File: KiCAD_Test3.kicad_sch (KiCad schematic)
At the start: 0 parts

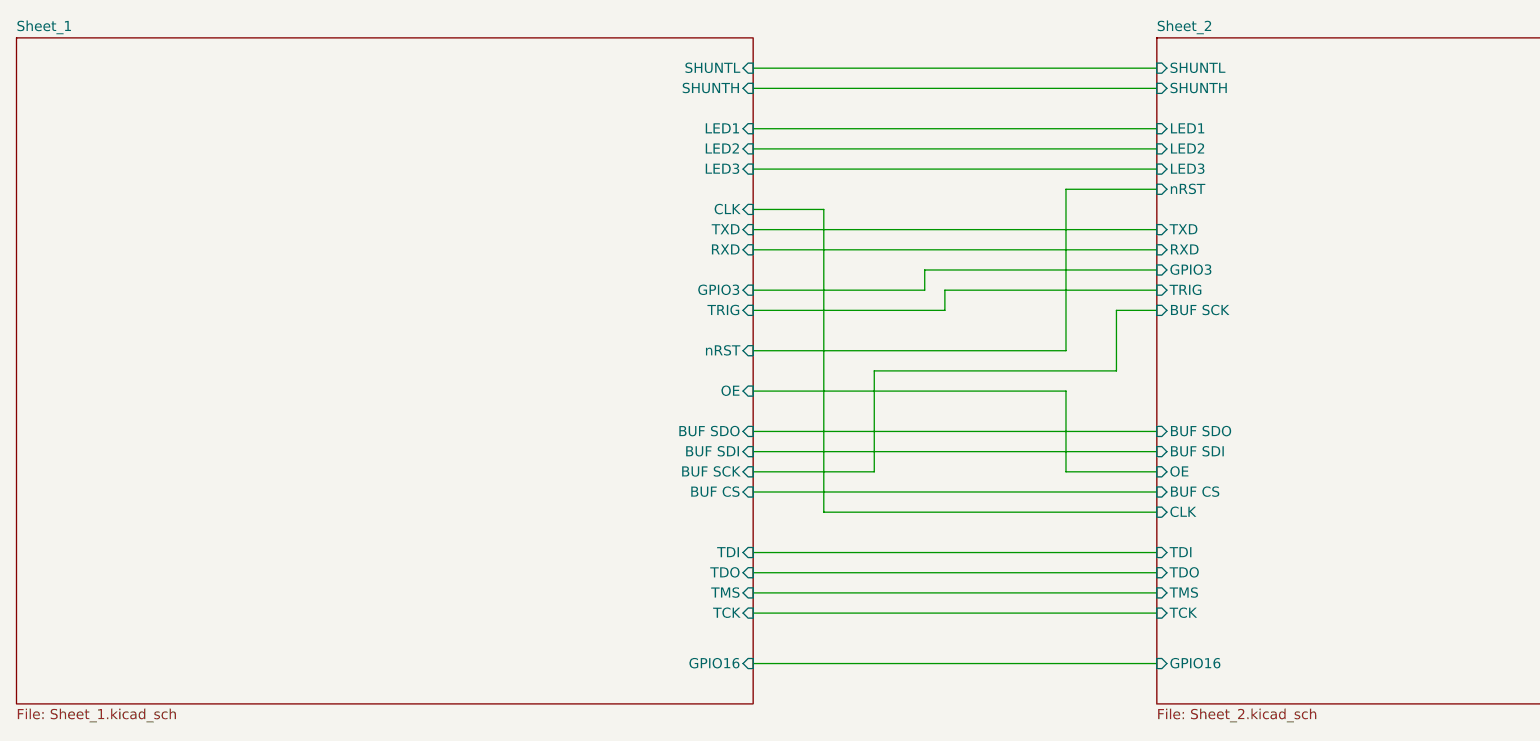
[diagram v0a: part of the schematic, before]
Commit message: updated ESP32 design - needs silkscreen added and shunt should be moved to be closer to U1
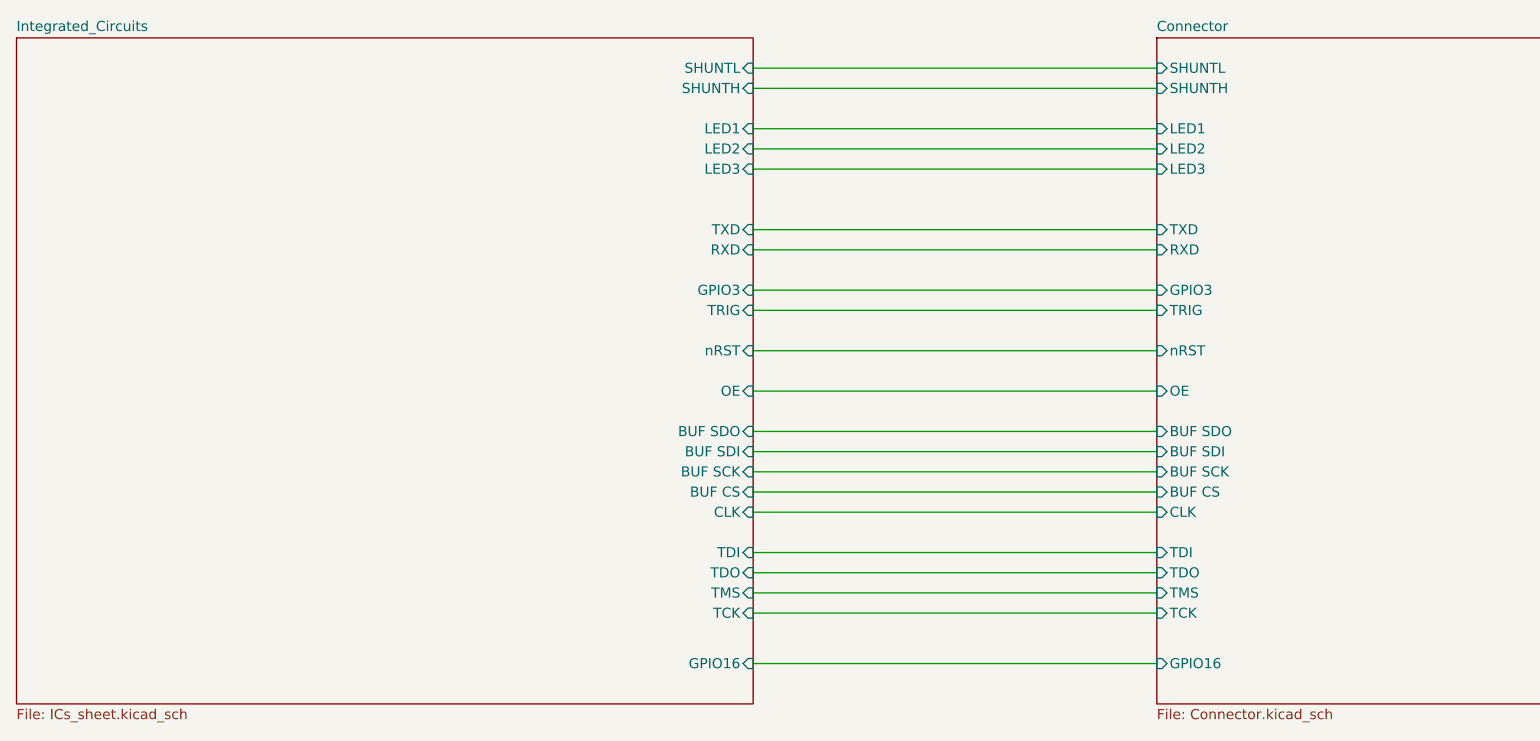
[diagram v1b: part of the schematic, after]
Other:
- sheet Sheet_1 renamed Integrated_Circuits
- sheet Sheet_2 renamed Connector
- sheet Connector: file Sheet_2.kicad_sch -> Connector.kicad_sch
- sheet Integrated_Circuits: file Sheet_1.kicad_sch -> ICs_sheet.kicad_sch
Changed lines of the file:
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@@
-	(wire
-		(pts
-			(xy 129.54 104.14) (xy 171.45 104.14)
-		)
-		(stroke
-			(width 0)
-			(type default)
-		)
-	)
 	(wire
 		(pts
@@
 	(wire
 		(pts
-			(xy 166.37 86.36) (xy 166.37 78.74)
-		)
-		(stroke
-			(width 0)
-			(type default)
-		)
-	)
-	(wire
-		(pts
-			(xy 135.89 86.36) (xy 166.37 86.36)
-		)
-		(stroke
-			(width 0)
-			(type default)
-		)
-	)
-	(wire
-		(pts
 			(xy 120.65 71.12) (xy 171.45 71.12)
 		)
@@
 	(wire
 		(pts
-			(xy 120.65 83.82) (xy 160.02 83.82)
+			(xy 120.65 83.82) (xy 171.45 83.82)
 		)
 		(stroke
@@
 	(wire
 		(pts
-			(xy 144.78 78.74) (xy 144.78 76.2)
-		)
-		(stroke
-			(width 0)
-			(type default)
-		)
-	)
-	(wire
-		(pts
 			(xy 120.65 109.22) (xy 171.45 109.22)
 		)
@@
 	(wire
 		(pts
-			(xy 120.65 78.74) (xy 144.78 78.74)
-		)
-		(stroke
-			(width 0)
-			(type default)
-		)
-	)
-	(wire
-		(pts
-			(xy 135.89 99.06) (xy 135.89 86.36)
-		)
-		(stroke
-			(width 0)
-			(type default)
-		)
-	)
-	(wire
-		(pts
-			(xy 120.65 66.04) (xy 129.54 66.04)
-		)
-		(stroke
-			(width 0)
-			(type default)
-		)
-	)
-	(wire
-		(pts
-			(xy 142.24 73.66) (xy 171.45 73.66)
+			(xy 120.65 78.74) (xy 171.45 78.74)
+		)
+		(stroke
+			(width 0)
+			(type default)
+		)
+	)
+	(wire
+		(pts
+			(xy 120.65 104.14) (xy 171.45 104.14)
 		)
 		(stroke
@@
 	(wire
 		(pts
-			(xy 160.02 99.06) (xy 171.45 99.06)
-		)
-		(stroke
-			(width 0)
-			(type default)
-		)
-	)
-	(wire
-		(pts
-			(xy 160.02 88.9) (xy 160.02 99.06)
-		)
-		(stroke
-			(width 0)
-			(type default)
-		)
-	)
-	(wire
-		(pts
 			(xy 120.65 60.96) (xy 171.45 60.96)
 		)
@@
 	(wire
 		(pts
-			(xy 160.02 63.5) (xy 160.02 83.82)
-		)
-		(stroke
-			(width 0)
-			(type default)
-		)
-	)
-	(wire
-		(pts
 			(xy 120.65 101.6) (xy 171.45 101.6)
 		)
@@
 	(wire
 		(pts
-			(xy 120.65 88.9) (xy 160.02 88.9)
-		)
-		(stroke
-			(width 0)
-			(type default)
-		)
-	)
-	(wire
-		(pts
-			(xy 129.54 66.04) (xy 129.54 104.14)
+			(xy 120.65 88.9) (xy 171.45 88.9)
 		)
 		(stroke
@@
 	(wire
 		(pts
-			(xy 160.02 63.5) (xy 171.45 63.5)
-		)
-		(stroke
-			(width 0)
-			(type default)
-		)
-	)
-	(wire
-		(pts
 			(xy 120.65 50.8) (xy 171.45 50.8)
 		)
@@
 	(wire
 		(pts
-			(xy 142.24 76.2) (xy 142.24 73.66)
-		)
-		(stroke
-			(width 0)
-			(type default)
-		)
-	)
-	(wire
-		(pts
-			(xy 120.65 76.2) (xy 142.24 76.2)
-		)
-		(stroke
-			(width 0)
-			(type default)
-		)
-	)
-	(wire
-		(pts
-			(xy 144.78 76.2) (xy 171.45 76.2)
+			(xy 120.65 76.2) (xy 171.45 76.2)
 		)
 		(stroke
@@
 	(wire
 		(pts
-			(xy 120.65 99.06) (xy 135.89 99.06)
-		)
-		(stroke
-			(width 0)
-			(type default)
-		)
-	)
-	(wire
-		(pts
-			(xy 166.37 78.74) (xy 171.45 78.74)
+			(xy 120.65 99.06) (xy 171.45 99.06)
 		)
 		(stroke
@@
 			(color 0 0 0 0.0000)
 		)
-		(property "Sheetname" "Sheet_1"
+		(property "Sheetname" "Integrated_Circuits"
 			(at 27.94 43.7384 0)
 			(effects
@@
 			)
 		)
-		(property "Sheetfile" "Sheet_1.kicad_sch"
+		(property "Sheetfile" "ICs_sheet.kicad_sch"
 			(at 27.94 128.8546 0)
 			(effects
@@
 		)
 		(pin "CLK" input
-			(at 120.65 66.04 0)
+			(at 120.65 104.14 0)
 			(effects
 				(font
@@
 			(color 0 0 0 0.0000)
 		)
-		(property "Sheetname" "Sheet_2"
+		(property "Sheetname" "Connector"
 			(at 171.45 43.7384 0)
 			(effects
@@
 			)
 		)
-		(property "Sheetfile" "Sheet_2.kicad_sch"
+		(property "Sheetfile" "Connector.kicad_sch"
 			(at 171.45 128.8546 0)
 			(effects
@@
 		)
 		(pin "nRST" input
-			(at 171.45 63.5 180)
+			(at 171.45 83.82 180)
 			(effects
 				(font
@@
 		)
 		(pin "GPIO3" input
-			(at 171.45 73.66 180)
+			(at 171.45 76.2 180)
 			(effects
 				(font
@@
 		)
 		(pin "TRIG" input
-			(at 171.45 76.2 180)
+			(at 171.45 78.74 180)
 			(effects
 				(font
@@
 		)
 		(pin "BUF SCK" input
-			(at 171.45 78.74 180)
+			(at 171.45 99.06 180)
 			(effects
 				(font
@@
 		)
 		(pin "OE" input
-			(at 171.45 99.06 180)
-			(effects
-				(font
+			(at 171.45 88.9 180)
+			(effects
+				(font

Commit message: updated design for esp32
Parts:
- added PCB1: CE, Silkscrren_Symbols:CE-Logo_8.5x6mm_SilkScreen, symbol Silkscreen_Symbols:CE_Free
- added PCB2: Pb_Free, Silkscrren_Symbols:Pb_Free_8.0x8.0mm_SilkScreen, symbol Silkscreen_Symbols:Pb_Free
- added PCB3: WEEE, Silkscrren_Symbols:WEEE-Logo_8.4x12mm_SilkScreen, symbol Silkscreen_Symbols:WEEE
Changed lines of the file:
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@@
+		)
+	)
+	(symbol
+		(lib_id "Silkscreen_Symbols:WEEE")
+		(at 27.94 179.07 0)
+		(unit 1)
+		(exclude_from_sim no)
+		(in_bom no)
+		(on_board yes)
+		(dnp no)
+		(fields_autoplaced yes)
+		(property "Reference" "PCB3"
+			(at 26.67 174.625 0)
+			(effects
+				(font
+					(size 1.27 1.27)
+				)
+				(hide yes)
+			)
+		)
+		(property "Value" "WEEE"
+			(at 27.94 179.07 0)
+			(effects
+				(font
+					(size 1.27 1.27)
+				)
+				(hide yes)
+			)
+		)
+		(property "Footprint" "Silkscrren_Symbols:WEEE-Logo_8.4x12mm_SilkScreen"
+			(at 27.94 179.07 0)
+			(effects
+				(font
+					(size 1.27 1.27)
+				)
+				(hide yes)
+			)
+		)
+		(property "Datasheet" ""
+			(at 27.94 179.07 0)
+			(effects
+				(font
+					(size 1.27 1.27)
+				)
+				(hide yes)
+			)
+		)
+		(property "Description" ""
+			(at 27.94 179.07 0)
+			(effects
+				(font
+					(size 1.27 1.27)
+				)
+				(hide yes)
+			)
+		)
+		(instances
+			(project ""
+				(path "/3a5d4ac2-6e78-4735-b22c-b99217f3b036"
+					(reference "PCB3")
+					(unit 1)
+				)
+			)
+		)
+	)
+	(symbol
+		(lib_id "Silkscreen_Symbols:CE_Free")
+		(at 27.94 156.21 0)
+		(unit 1)
+		(exclude_from_sim no)
+		(in_bom no)
+		(on_board yes)
+		(dnp no)
+		(fields_autoplaced yes)
+		(property "Reference" "PCB1"
+			(at 25.4 149.86 0)
+			(effects
+				(font
+					(size 1.27 1.27)
+				)
+				(hide yes)
+			)
+		)
+		(property "Value" "CE"
+			(at 27.94 156.21 0)
+			(effects
+				(font
+					(size 1.27 1.27)
+				)
+				(hide yes)
+			)
+		)
+		(property "Footprint" "Silkscrren_Symbols:CE-Logo_8.5x6mm_SilkScreen"
+			(at 27.94 156.21 0)
+			(effects
+				(font
+					(size 1.27 1.27)
+				)
+				(hide yes)
+			)
+		)
+		(property "Datasheet" ""
+			(at 27.94 156.21 0)
+			(effects
+				(font
+					(size 1.27 1.27)
+				)
+				(hide yes)
+			)
+		)
+		(property "Description" ""
+			(at 27.94 156.21 0)
+			(effects
+				(font
+					(size 1.27 1.27)
+				)
+				(hide yes)
+			)
+		)
+		(instances
+			(project ""
+				(path "/3a5d4ac2-6e78-4735-b22c-b99217f3b036"
+					(reference "PCB1")
+					(unit 1)
+				)
+			)
+		)
+	)
+	(symbol
+		(lib_id "Silkscreen_Symbols:Pb_Free")
+		(at 21.59 167.64 0)
+		(unit 1)
+		(exclude_from_sim no)
+		(in_bom no)
+		(on_board yes)
+		(dnp no)
+		(fields_autoplaced yes)
+		(property "Reference" "PCB2"
+			(at 21.59 167.64 0)
+			(effects
+				(font
+					(size 1.27 1.27)
+				)
+				(hide yes)
+			)
+		)
+		(property "Value" "Pb_Free"
+			(at 21.59 167.64 0)
+			(effects
+				(font
+					(size 1.27 1.27)
+				)
+				(hide yes)
+			)
+		)
+		(property "Footprint" "Silkscrren_Symbols:Pb_Free_8.0x8.0mm_SilkScreen"
+			(at 21.59 167.64 0)
+			(effects
+				(font
+					(size 1.27 1.27)
+				)
+				(hide yes)
+			)
+		)
+		(property "Datasheet" ""
+			(at 21.59 167.64 0)
+			(effects
+				(font
+					(size 1.27 1.27)
+				)
+				(hide yes)
+			)
+		)
+		(property "Description" ""
+			(at 21.59 167.64 0)
+			(effects
+				(font
+					(size 1.27 1.27)
+				)
+				(hide yes)
+			)
+		)
+		(instances
+			(project ""
+				(path "/3a5d4ac2-6e78-4735-b22c-b99217f3b036"
+					(reference "PCB2")
+					(unit 1)
+				)
+			)
 		)
 	)

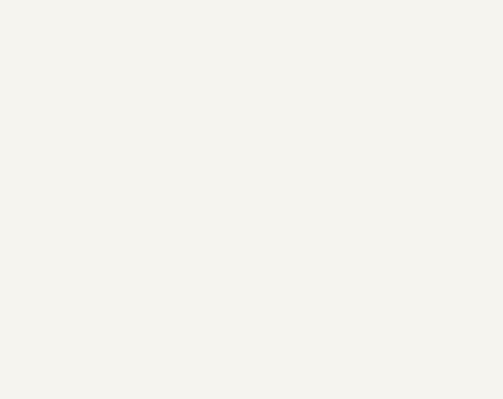
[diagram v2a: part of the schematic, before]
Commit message: updated design - removed visible pin numbers from passives, fixed connections, updated silkscreen
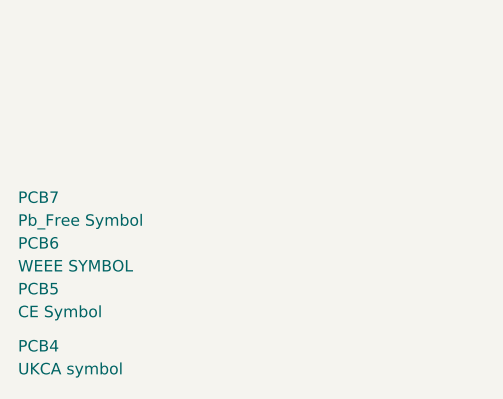
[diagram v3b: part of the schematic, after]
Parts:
- removed PCB1: CE, Silkscrren_Symbols:CE-Logo_8.5x6mm_SilkScreen, symbol Silkscreen_Symbols:CE_Free
- removed PCB2: Pb_Free, Silkscrren_Symbols:Pb_Free_8.0x8.0mm_SilkScreen, symbol Silkscreen_Symbols:Pb_Free
- removed PCB3: WEEE, Silkscrren_Symbols:WEEE-Logo_8.4x12mm_SilkScreen, symbol Silkscreen_Symbols:WEEE
- added PCB4: UKCA symbol, Silkscrren_Symbols:UKCA-Logo_8x8mm_SilkScreen, symbol Silkscreen_Symbols:UKCA
- added PCB5: CE Symbol, Silkscrren_Symbols:CE-Logo_8.5x6mm_SilkScreen, symbol Silkscreen_Symbols:CE_Free
- added PCB6: WEEE SYMBOL, Silkscrren_Symbols:WEEE-Logo_5.6x8mm_SilkScreen, symbol Silkscreen_Symbols:WEEE
- added PCB7: Pb_Free Symbol, Silkscrren_Symbols:Pb_Free_8.0x8.0mm_SilkScreen, symbol Silkscreen_Symbols:Pb_Free
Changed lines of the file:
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@@
+	)
+	(symbol
+		(lib_id "Silkscreen_Symbols:CE_Free")
+		(at -52.07 175.26 0)
+		(unit 1)
+		(exclude_from_sim no)
+		(in_bom no)
+		(on_board yes)
+		(dnp no)
+		(fields_autoplaced yes)
+		(property "Reference" "PCB5"
+			(at -49.53 173.9899 0)
+			(effects
+				(font
+					(size 1.27 1.27)
+				)
+				(justify left)
+			)
+		)
+		(property "Value" "CE Symbol"
+			(at -49.53 176.5299 0)
+			(effects
+				(font
+					(size 1.27 1.27)
+				)
+				(justify left)
+			)
+		)
+		(property "Footprint" "Silkscrren_Symbols:CE-Logo_8.5x6mm_SilkScreen"
+			(at -52.07 175.26 0)
+			(effects
+				(font
+					(size 1.27 1.27)
+				)
+				(hide yes)
+			)
+		)
+		(property "Datasheet" ""
+			(at -52.07 175.26 0)
+			(effects
+				(font
+					(size 1.27 1.27)
+				)
+				(hide yes)
+			)
+		)
+		(property "Description" ""
+			(at -52.07 175.26 0)
+			(effects
+				(font
+					(size 1.27 1.27)
+				)
+				(hide yes)
+			)
+		)
+		(instances
+			(project ""
+				(path "/3a5d4ac2-6e78-4735-b22c-b99217f3b036"
+					(reference "PCB5")
+					(unit 1)
+				)
+			)
+		)
+	)
+	(symbol
+		(lib_id "Silkscreen_Symbols:Pb_Free")
+		(at -52.07 165.1 0)
+		(unit 1)
+		(exclude_from_sim no)
+		(in_bom no)
+		(on_board yes)
+		(dnp no)
+		(fields_autoplaced yes)
+		(property "Reference" "PCB7"
+			(at -49.53 163.8299 0)
+			(effects
+				(font
+					(size 1.27 1.27)
+				)
+				(justify left)
+			)
+		)
+		(property "Value" "Pb_Free Symbol"
+			(at -49.53 166.3699 0)
+			(effects
+				(font
+					(size 1.27 1.27)
+				)
+				(justify left)
+			)
+		)
+		(property "Footprint" "Silkscrren_Symbols:Pb_Free_8.0x8.0mm_SilkScreen"
+			(at -52.07 165.1 0)
+			(effects
+				(font
+					(size 1.27 1.27)
+				)
+				(hide yes)
+			)
+		)
+		(property "Datasheet" ""
+			(at -52.07 165.1 0)
+			(effects
+				(font
+					(size 1.27 1.27)
+				)
+				(hide yes)
+			)
+		)
+		(property "Description" ""
+			(at -52.07 165.1 0)
+			(effects
+				(font
+					(size 1.27 1.27)
+				)
+				(hide yes)
+			)
+		)
+		(instances
+			(project ""
+				(path "/3a5d4ac2-6e78-4735-b22c-b99217f3b036"
+					(reference "PCB7")
+					(unit 1)
+				)
+			)
+		)
+	)
+	(symbol
+		(lib_id "Silkscreen_Symbols:UKCA")
+		(at -52.07 181.61 0)
+		(unit 1)
+		(exclude_from_sim no)
+		(in_bom yes)
+		(on_board yes)
+		(dnp no)
+		(fields_autoplaced yes)
+		(property "Reference" "PCB4"
+			(at -49.53 180.3399 0)
+			(effects
+				(font
+					(size 1.27 1.27)
+				)
+				(justify left)
+			)
+		)
+		(property "Value" "UKCA symbol"
+			(at -49.53 182.8799 0)
+			(effects
+				(font
+					(size 1.27 1.27)
+				)
+				(justify left)
+			)
+		)
+		(property "Footprint" "Silkscrren_Symbols:UKCA-Logo_8x8mm_SilkScreen"
+			(at -52.07 181.61 0)
+			(effects
+				(font
+					(size 1.27 1.27)
+				)
+				(hide yes)
+			)
+		)
+		(property "Datasheet" ""
+			(at -52.07 181.61 0)
+			(effects
+				(font
+					(size 1.27 1.27)
+				)
+				(hide yes)
+			)
+		)
+		(property "Description" ""
+			(at -52.07 181.61 0)
+			(effects
+				(font
+					(size 1.27 1.27)
+				)
+				(hide yes)
+			)
+		)
+		(instances
+			(project ""
+				(path "/3a5d4ac2-6e78-4735-b22c-b99217f3b036"
+					(reference "PCB4")
+					(unit 1)
+				)
+			)
+		)
 	)
 	(symbol
 		(lib_id "Silkscreen_Symbols:WEEE")
-		(at 27.94 179.07 0)
+		(at -52.07 170.18 0)
 		(unit 1)
 		(exclude_from_sim no)
@@
 		(dnp no)
 		(fields_autoplaced yes)
-		(property "Reference" "PCB3"
-			(at 26.67 174.625 0)
-			(effects
-				(font
-					(size 1.27 1.27)
-				)
-				(hide yes)
-			)
-		)
-		(property "Value" "WEEE"
-			(at 27.94 179.07 0)
-			(effects
-				(font
-					(size 1.27 1.27)
-				)
-				(hide yes)
-			)
-		)
-		(property "Footprint" "Silkscrren_Symbols:WEEE-Logo_8.4x12mm_SilkScreen"
-			(at 27.94 179.07 0)
-			(effects
-				(font
-					(size 1.27 1.27)
-				)
-				(hide yes)
-			)
-		)
-		(property "Datasheet" ""
-			(at 27.94 179.07 0)
-			(effects
-				(font
-					(size 1.27 1.27)
-				)
-				(hide yes)
-			)
-		)
-		(property "Description" ""
-			(at 27.94 179.07 0)
-			(effects
-				(font
-					(size 1.27 1.27)
-				)
-				(hide yes)
-			)
-		)
-		(instances
-			(project ""
-				(path "/3a5d4ac2-6e78-4735-b22c-b99217f3b036"
-					(reference "PCB3")
-					(unit 1)
-				)
-			)
-		)
-	)
-	(symbol
-		(lib_id "Silkscreen_Symbols:CE_Free")
-		(at 27.94 156.21 0)
-		(unit 1)
-		(exclude_from_sim no)
-		(in_bom no)
-		(on_board yes)
-		(dnp no)
-		(fields_autoplaced yes)
-		(property "Reference" "PCB1"
-			(at 25.4 149.86 0)
-			(effects
-				(font
-					(size 1.27 1.27)
-				)
-				(hide yes)
-			)
-		)
-		(property "Value" "CE"
-			(at 27.94 156.21 0)
-			(effects
-				(font
-					(size 1.27 1.27)
-				)
-				(hide yes)
-			)
-		)
-		(property "Footprint" "Silkscrren_Symbols:CE-Logo_8.5x6mm_SilkScreen"
-			(at 27.94 156.21 0)
-			(effects
-				(font
-					(size 1.27 1.27)
-				)
-				(hide yes)
-			)
-		)
-		(property "Datasheet" ""
-			(at 27.94 156.21 0)
-			(effects
-				(font
-					(size 1.27 1.27)
-				)
-				(hide yes)
-			)
-		)
-		(property "Description" ""
-			(at 27.94 156.21 0)
-			(effects
-				(font
-					(size 1.27 1.27)
-				)
-				(hide yes)
-			)
-		)
-		(instances
-			(project ""
-				(path "/3a5d4ac2-6e78-4735-b22c-b99217f3b036"
-					(reference "PCB1")
-					(unit 1)
-				)
-			)
-		)
-	)
-	(symbol
-		(lib_id "Silkscreen_Symbols:Pb_Free")
-		(at 21.59 167.64 0)
-		(unit 1)
-		(exclude_from_sim no)
-		(in_bom no)
-		(on_board yes)
-		(dnp no)
-		(fields_autoplaced yes)
-		(property "Reference" "PCB2"
-			(at 21.59 167.64 0)
-			(effects
-				(font
-					(size 1.27 1.27)
-				)
-				(hide yes)
-			)
-		)
-		(property "Value" "Pb_Free"
-			(at 21.59 167.64 0)
-			(effects
-				(font
-					(size 1.27 1.27)
-				)
-				(hide yes)
-			)
-		)
-		(property "Footprint" "Silkscrren_Symbols:Pb_Free_8.0x8.0mm_SilkScreen"
-			(at 21.59 167.64 0)
-			(effects
-				(font
-					(size 1.27 1.27)
-				)
-				(hide yes)
-			)
-		)
-		(property "Datasheet" ""
-			(at 21.59 167.64 0)
-			(effects
-				(font
-					(size 1.27 1.27)
-				)
-				(hide yes)
-			)
-		)
-		(property "Description" ""
-			(at 21.59 167.64 0)
-			(effects
-				(font
-					(size 1.27 1.27)
-				)
-				(hide yes)
-			)
-		)
-		(instances
-			(project ""
-				(path "/3a5d4ac2-6e78-4735-b22c-b99217f3b036"
-					(reference "PCB2")
-					(unit 1)
-				)
+		(property "Reference" "PCB6"
+			(at -49.53 168.9099 0)
+			(effects
+				(font
+					(size 1.27 1.27)
+				)
+				(justify left)
+			)
+		)
+		(property "Value" "WEEE SYMBOL"
+			(at -49.53 171.4499 0)
+			(effects
+				(font
+					(size 1.27 1.27)
+				)
+				(justify left)
+			)
+		)
+		(property "Footprint" "Silkscrren_Symbols:WEEE-Logo_5.6x8mm_SilkScreen"
+			(at -52.07 170.18 0)
+			(effects
+				(font
+					(size 1.27 1.27)
+				)
+				(hide yes)
+			)
+		)
+		(property "Datasheet" ""
+			(at -52.07 170.18 0)
+			(effects
+				(font
+					(size 1.27 1.27)
+				)
+				(hide yes)
+			)
+		)
+		(property "Description" ""
+			(at -52.07 170.18 0)
+			(effects
+				(font
+					(size 1.27 1.27)
+				)
+				(hide yes)
+			)
+		)
+		(instances
+			(project ""
+				(path "/3a5d4ac2-6e78-4735-b22c-b99217f3b036"
+					(reference "PCB6")
+					(unit 1)
+				)
